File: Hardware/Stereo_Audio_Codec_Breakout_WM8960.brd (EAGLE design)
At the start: 25.4 x 64.8 mm, 36 parts, among them J1 QWIIC, J2 AUDIO_JACK_3.5MM_SMD, U4 WM8960, Y1 24 MHz

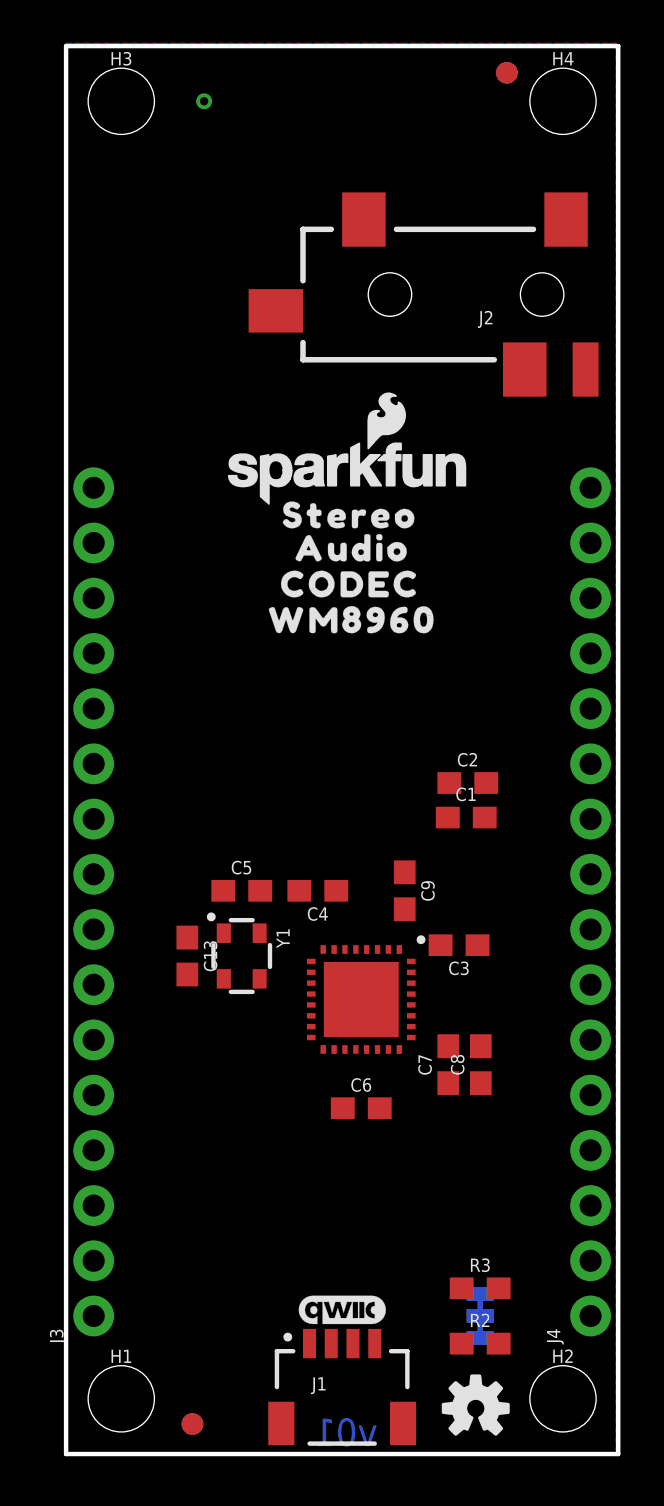
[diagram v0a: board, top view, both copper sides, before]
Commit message: Breakout routed ready for proto review
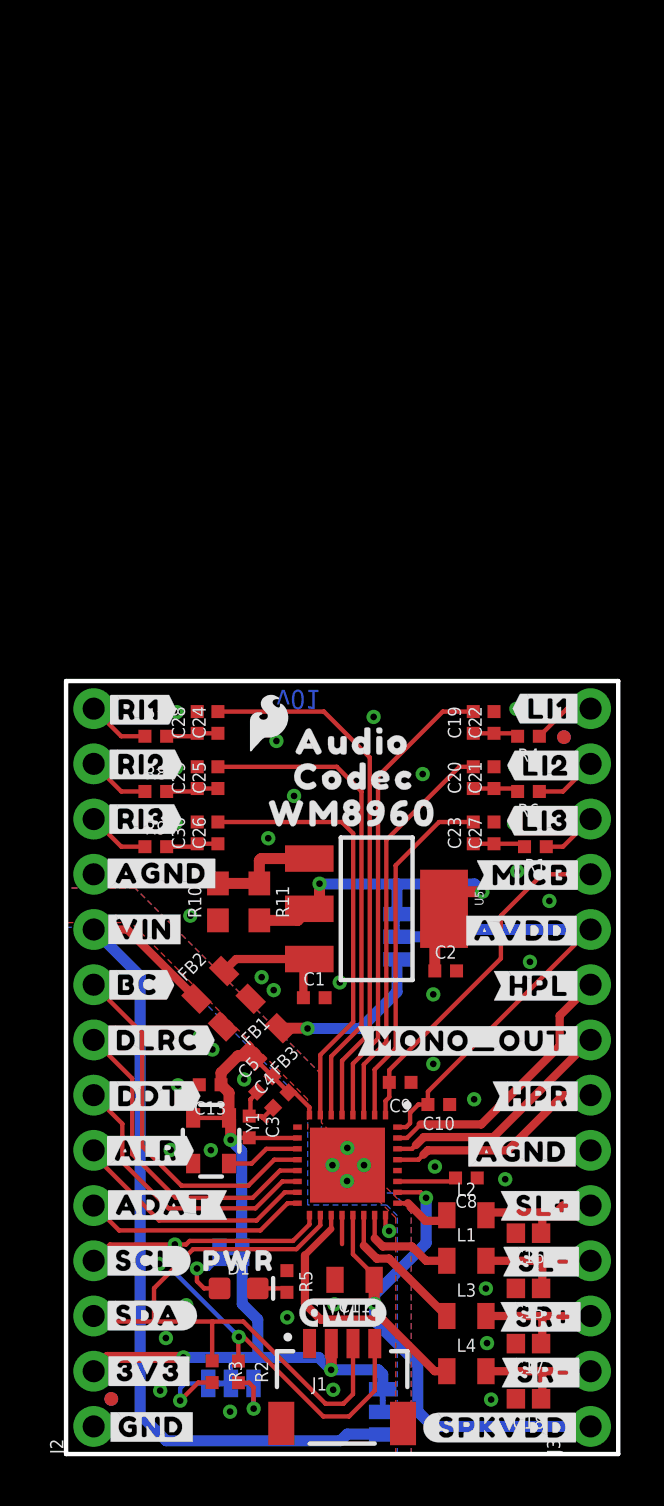
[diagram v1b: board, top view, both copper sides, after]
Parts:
- removed C6, C7: 4.7uF, SparkFun-Capacitors:0603
- removed H1, H2, H3, H4: STAND-OFFTIGHT, SparkFun-Hardware:STAND-OFF-TIGHT
- removed J4: (no value), SparkFun-Connectors:1X16_NO_SILK
- removed LOGO2: SFE_LOGO_NAME_FLAME.1_INCH, SparkFun-Aesthetics:SFE_LOGO_NAME_FLAME_.1
- removed U$8: (no value), buzzard_labels (17):I2C3
- added AVDD, SPKVDD: (no value), SparkFun-Jumpers:SMT-JUMPER_3_1-NC_TRACE_SILK
- added C10: 0.1uF, SparkFun-Capacitors:0402-TIGHT
- added C11: 10uF, SparkFun-Capacitors:0805
- added C15, C16, C17, C18: 1nF, SparkFun-Capacitors:0402
- added C19, C20, C23, C24, C25, C26: 1.0uF, SparkFun-Capacitors:0402-TIGHT
- added C21, C22, C27, C28, C29, C30: 47nF, SparkFun-Capacitors:0402-TIGHT
- added D1: RED, SparkFun-LED:LED-0603
- added FB1, FB2, FB3: 600Ω, SparkFun-Coils:0805
- added L1, L2, L3, L4: 220Ω, SparkFun-Coils:0805
- added LED: (no value), SparkFun-Jumpers:SMT-JUMPER_2_NC_TRACE_SILK
- added LOGO1: SFE_LOGO_NAME_FLAMEBLANK, SparkFun-Aesthetics:BLANK
- added R1, R4, R6, R7, R8, R9: 100, SparkFun-Resistors:0402-TIGHT
- added R10: 390, SparkFun-Resistors:0603
- added R11: 240, SparkFun-Resistors:0603
- added R5: 1k, SparkFun-Resistors:0402-TIGHT
- added U$13: (no value), output:#SR##4
- added U$14: (no value), output:#SL##6
- added U$15: (no value), output:#SR##5
- added U$16: (no value), output:#SL##7
- added U$17: (no value), output:#SPKVDD#13
- added U$18, U$50: (no value), output:#GND#8
- added U$20: (no value), output:#RI1#10
- added U$21: (no value), output:#RI2#10
- added U$22: (no value), output:#RI3#10
- added U$23: (no value), output:#LI1#10
- added U$24: (no value), output:#LI2#10
- added U$25: (no value), output:#LI3#10
- added U$26: (no value), output:#HPL#10
- added U$27: (no value), output:#HPR#11
- added U$28, U$51: (no value), output:#3V3#12
- added U$29: (no value), SparkFun-Aesthetics:SFE_LOGO_FLAME_.1
- added U$35: (no value), output:PWR12
- added U$36: (no value), output:WM8960896054
- added U$38: (no value), output:#3V3#17
- added U$39: (no value), output:#LED#17
- added U$40: (no value), output:#I2C#18
- added U$41, U$42, U$43, U$44: (no value), output:#AGND#18
- added U$45, U$46: (no value), output:#VIN#19
- added U$47: (no value), output:#MONO_OUT#20
- added U$48, U$49: (no value), output:#AVDD#22
- added U$52: (no value), output:#BC#24
- added U$53: (no value), output:#DLRC#25
- added U$54: (no value), output:#ADAT#26
- added U$55: (no value), output:#SCL#27
- added U$56: (no value), output:#SDA#28
- added U$57: (no value), output:#ALR#29
- added U$58: (no value), output:#DDT#30
- added U$59: (no value), output:#MICB#31
- added U$60: (no value), output:WM89600
- added U$61: (no value), output:AUDIO0
- added U$63: (no value), output:AVDD32
- added U$64: (no value), output:#SPKVDD#51
- added U$65: (no value), output:#3V3#35
- added U$66: (no value), output:#RINPUT1#35
- added U$67: (no value), output:#RINPUT2#35
- added U$68: (no value), output:#RINPUT3#35
- added U$69: (no value), output:#BCLK#35
- added U$70: (no value), output:#DACLRC#36
- added U$71: (no value), output:#DACDAT#37
- added U$72: (no value), output:#ADCLRC#38
- added U$73: (no value), output:#ADCDAT#39
- added U$74: (no value), output:#SCL#40
- added U$75: (no value), output:#SDA#41
- added U$76: (no value), output:#LINPUT1#42
- added U$77: (no value), output:#LINPUT2#42
- added U$78: (no value), output:#LINPUT3#42
- added U$79: (no value), output:#MICBIAS#42
- added U$80: (no value), output:#HPL#43
- added U$81: (no value), output:#MONO_OUT#44
- added U$82: (no value), output:#HPR#45
- added U$83: (no value), output:#SPK_LP#46
- added U$84: (no value), output:#SPK_LN#47
- added U$85: (no value), output:#SPK_RP#48
- added U$86: (no value), output:#SPK_RN#49
- added U$87: (no value), output:#REG#50
- added U$88: (no value), output:#VIN#52
- added U5: LM1117, SparkFun-IC-Power:SOT223
- C1: value 2.2uF -> 0.1uF; device SparkFun-Capacitors:0603 -> SparkFun-Capacitors:0402-TIGHT
- C13, C3, C4, C5, C8, C9: device SparkFun-Capacitors:0603 -> SparkFun-Capacitors:0402-TIGHT
- C2: value 2.2uF -> 10uF; device SparkFun-Capacitors:0603 -> SparkFun-Capacitors:0402-TIGHT
- FD1, FD2, FD3, FD4: value FIDUCIAL1X2 -> FIDUCIALUFIDUCIAL; device SparkFun-Aesthetics:FIDUCIAL-1X2 -> SparkFun-Aesthetics:FIDUCIAL-MICRO
- J2: value AUDIO_JACK_3.5MM_SMD -> (none); device SparkFun-Connectors:AUDIO-JACK-3.5MM-SMD -> SparkFun-Connectors:1X14_NO_SILK
- J3: device SparkFun-Connectors:1X16_NO_SILK -> SparkFun-Connectors:1X14_NO_SILK
- R2, R3: value 4.7k -> 2.2k; device SparkFun-Resistors:0603 -> SparkFun-Resistors:0402-TIGHT
- U$1: device output:WM89600 -> output:AUDIO8960896055
- U$2: device output:AUDIO0 -> output:CODEC8960896056
- U$3: device output:CODEC0 -> output:CODEC8960896057
- U$4: device output:STEREO0 -> SparkFun-Aesthetics:SFE_LOGO_FLAME_.1
- moved J2 57.4 mm to (1.27, 1.27), turned to 90 degrees
- moved FD3 30.7 mm to (22.9, 33.0), turned to 180 degrees
- moved FD4 30.7 mm to (22.9, 33.0), turned to 180 degrees
- moved J3 23.4 mm to (24.1, 1.27)
- moved R3 12.9 mm to (6.72, 3.79), turned to 270 degrees
- moved C3 12.8 mm to (8.42, 15.0), turned to 270 degrees
- moved I2C 11.9 mm to (7.58, 3.25), turned to 180 degrees
- moved U$2 11.5 mm to (12.8, 30.2), flipped to the bottom
- moved R2 11.2 mm to (7.92, 3.78), turned to 270 degrees
- moved C1 10.8 mm to (11.4, 21.0)
- moved U$4 10.8 mm to (14.0, 32.4), flipped to the bottom
- moved C4 9.78 mm to (9.88, 16.3), turned to 45 degrees
- moved C5 8.95 mm to (9.14, 17.0), turned to 45 degrees
- moved U$3 8.86 mm to (13.3, 31.2)
- moved C9 8.82 mm to (15.4, 17.1), turned to 180 degrees
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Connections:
- removed net 5V: C6.2, C7.2, U4.21, U4.26
- removed net ADC-DAT: U4.16
- removed net DAC-DAT: U4.14
- removed net DAC-LRC: U4.13, U4.15
- removed net GND: C13.2, C3.1, C4.1, C5.1, C6.1, C7.1, C8.1, C9.1, J1.1, U4.20, U4.24, U4.28, U4.9, U4.PADDLE, Y1.2
- new net ADCDAT: J2.5, U4.16
- new net ADCLRC: J2.6, U4.15
- new net AGND: C1.2, C10.1, C15.2, C16.2, C17.2, C18.2, C2.2, C21.2, C22.2, C27.2, C28.2, C29.2, C30.2, C8.1, C9.1, FB1.1, J2.11, J3.6, R10.1, U4.28, U4.PADDLE
- new net AVDD: AVDD.2, C10.2, J3.10, U4.32
- new net AVDD-REG: AVDD.3, C2.1, R11.2, U5.2, U5.4
- new net DACDAT: J2.7, U4.14
- new net DACLRC: J2.8, U4.13
- new net DGND: C11.2, C13.2, C3.1, C4.1, C5.1, FB1.2, J1.1, J2.1, R5.1, U4.20, U4.24, U4.9, Y1.2
- new net LINPUT2: J3.13, R6.1
- new net LINPUT3: J3.12, R1.1
- new net N$1: L3.1, U4.22
- new net N$13: C20.1, C21.1, R6.2
- new net N$14: C19.1, C22.1, R4.2
- new net N$15: C23.1, C27.1, R1.2
- new net N$18: C24.1, C28.1, R7.2
- new net N$19: C25.1, C29.1, R8.2
- new net N$2: AVDD.1, FB3.1
- new net N$20: C26.1, C30.1, R9.2
- new net N$25: R10.2, R11.1, U5.1
- new net N$3: L4.1, U4.19
- new net N$4: L2.1, U4.25
- new net N$45: C1.1, FB2.2, U5.3
- new net N$5: L1.1, U4.23
- new net N$6: D1.C, R5.2
- new net N$7: D1.A, LED.1
- new net RINPUT2: J2.13, R8.1
- new net RINPUT3: J2.12, R9.1
- new net SPKVDD: C11.1, J3.1, SPKVDD.2, U4.21, U4.26
- new net VIN: FB2.1, J2.10, SPKVDD.1
- net 3.3V: now also FB3.2, J2.2, LED.2, SPKVDD.3; no longer U4.32
- net BCLK: now also J2.9
- net HP_L: now also J3.9
- net HP_R: now also J3.7
- net LINPUT1: now also J3.14, R4.1; no longer C1.2
- net MICBIAS: now also J3.11
- net MONO_OUT: now also J3.8
- net N$10: now also C23.2
- net N$12: now also C20.2
- net N$29: now also C19.2; no longer C1.1
- net N$30: now also C24.2; no longer C2.1
- net N$8: now also C26.2
- net N$9: now also C25.2
- net RINPUT1: now also J2.14, R7.1; no longer C2.2
- net SCL: now also J2.4
- net SDA: now also J2.3
- net SPK_LN: now also C15.1, J3.4, L1.2; no longer U4.23
- net SPK_LP: now also C16.1, J3.5, L2.2; no longer U4.25
- net SPK_RN: now also C18.1, J3.2, L4.2; no longer U4.19
- net SPK_RP: now also C17.1, J3.3, L3.2; no longer U4.22
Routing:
- net 3.3V: track 0.00 -> 41.3 mm, vias 0 -> 3
- net VIN: track 0.00 -> 41.0 mm
- net SDA: track 0.00 -> 28.8 mm
- net SCL: track 0.00 -> 28.1 mm, vias 0 -> 2
- net SPKVDD: track 0.00 -> 27.4 mm, vias 0 -> 2
- net N$30: track 0.00 -> 24.8 mm
- net N$9: track 0.00 -> 22.5 mm
- net AVDD: track 0.00 -> 22.3 mm
- net N$29: track 0.00 -> 21.7 mm
- net N$8: track 0.00 -> 20.0 mm
- net AVDD-REG: track 0.00 -> 18.7 mm, vias 0 -> 2
- net N$12: track 0.00 -> 18.5 mm
- net BCLK: track 0.00 -> 16.7 mm
- net MICBIAS: track 0.00 -> 16.3 mm
- net N$10: track 0.00 -> 16.3 mm
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- added copper zone on layer 1, net AGND
- added copper zone on layer 16, net AGND
- added copper zone on layer 1, net DGND
- added copper zone on layer 16, net DGND
- removed copper zone on layer 1, net GND
- removed copper zone on layer 16, net GND
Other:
- board size 25.4 x 64.8 mm -> 25.4 x 35.6 mm

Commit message: Switched MONO OUT to OUT3, because that is a better name
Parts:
- removed U$47: (no value), output:#MONO_OUT#20
- removed U$81: (no value), output:#MONO_OUT#44
- added U$37: (no value), output:#OUT3#0
- added U$5: (no value), output:#OUT3#8960896058
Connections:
- net MONO_OUT renamed OUT3
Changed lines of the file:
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@@
 <setting verticaltext="up"/>
 </settings>
-<grid distance="0.025" unitdist="inch" unit="inch" style="lines" multiple="1" display="yes" altdistance="0.0001" altunitdist="inch" altunit="inch"/>
+<grid distance="0.05" unitdist="inch" unit="inch" style="lines" multiple="1" display="yes" altdistance="0.0001" altunitdist="inch" altunit="inch"/>
 <layers>
 <layer number="1" name="Top" color="4" fill="1" visible="yes" active="yes"/>
@@
 <element name="U$45" library="output" package="#VIN#19" value="" x="3.604259375" y="24.13761875" smashed="yes"/>
 <element name="U$46" library="output" package="#VIN#19" value="" x="3.596640625" y="24.127459375" smashed="yes" rot="MR0"/>
-<element name="U$47" library="output" package="#MONO_OUT#20" value="" x="18.641059375" y="19.00428125" smashed="yes"/>
 <element name="U$48" library="output" package="#AVDD#22" value="" x="20.94991875" y="24.0792" smashed="yes"/>
 <element name="U$49" library="output" package="#AVDD#22" value="" x="20.952459375" y="24.069040625" smashed="yes" rot="MR0"/>
@@
 <element name="U$79" library="output" package="#MICBIAS#42" value="" x="20.02281875" y="26.647140625" smashed="yes" rot="MR0"/>
 <element name="U$80" library="output" package="#HPL#43" value="" x="21.6535" y="21.605240625" smashed="yes" rot="MR0"/>
-<element name="U$81" library="output" package="#MONO_OUT#44" value="" x="18.50898125" y="19.034759375" smashed="yes" rot="MR0"/>
 <element name="U$82" library="output" package="#HPR#45" value="" x="21.57221875" y="16.393159375" smashed="yes" rot="MR0"/>
 <element name="U$83" library="output" package="#SPK_LP#46" value="" x="20.15998125" y="11.4173" smashed="yes" rot="MR0"/>
@@
 <element name="LOGO1" library="SparkFun-Aesthetics" package="BLANK" value="SFE_LOGO_NAME_FLAMEBLANK" x="-16.51" y="-16.51" smashed="yes"/>
 <element name="U$3" library="output" package="CODEC8960896057" value="" x="13.274040625" y="31.150559375" smashed="yes"/>
+<element name="U$5" library="output" package="#OUT3#8960896058" value="" x="21.082" y="19.05" smashed="yes"/>
+<element name="U$37" library="output" package="#OUT3#0" value="" x="20.977859375" y="19.022059375" smashed="yes" rot="MR0"/>
 </elements>
 <signals>
@@
 <wire x1="16.637" y1="13.97" x2="20.32" y2="13.97" width="0.381" layer="1"/>
 </signal>
-<signal name="MONO_OUT">
+<signal name="OUT3">
 <contactref element="U4" pad="30"/>
 <contactref element="J3" pad="8"/>
